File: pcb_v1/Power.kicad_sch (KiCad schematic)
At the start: 12 parts, among them J1 Conn_01x02, J2 Conn_01x04, U1 MAX17048G_T10, U5 TPB4056A20-ES1R

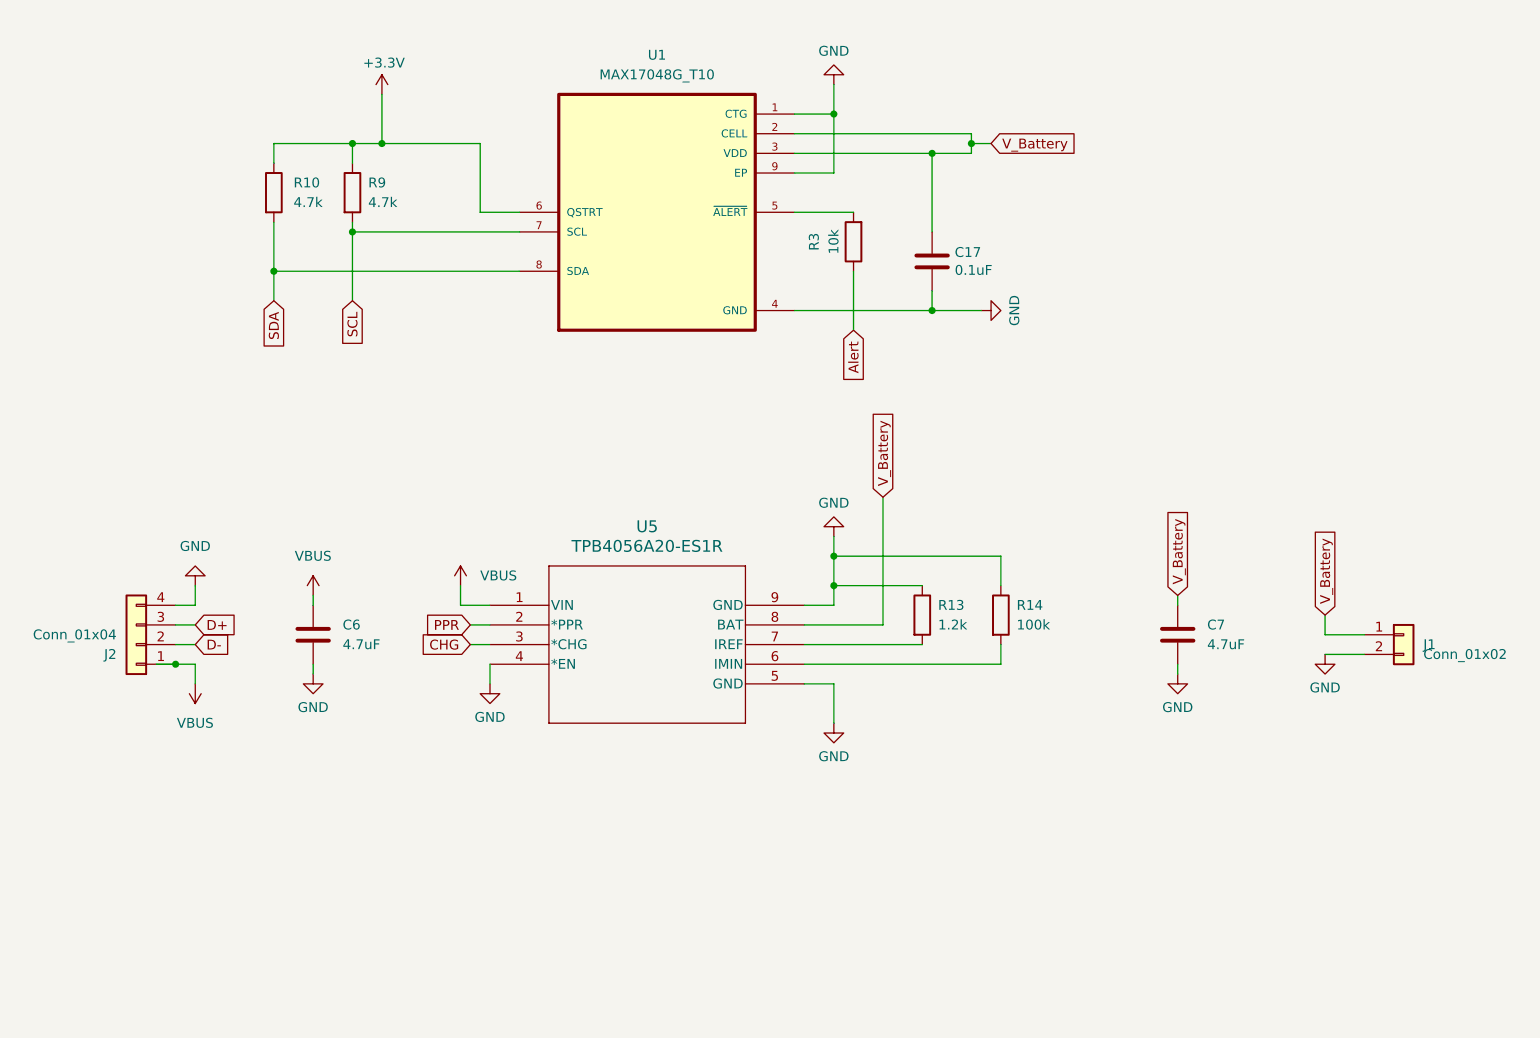
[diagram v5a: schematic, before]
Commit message: Finished 4 layer design
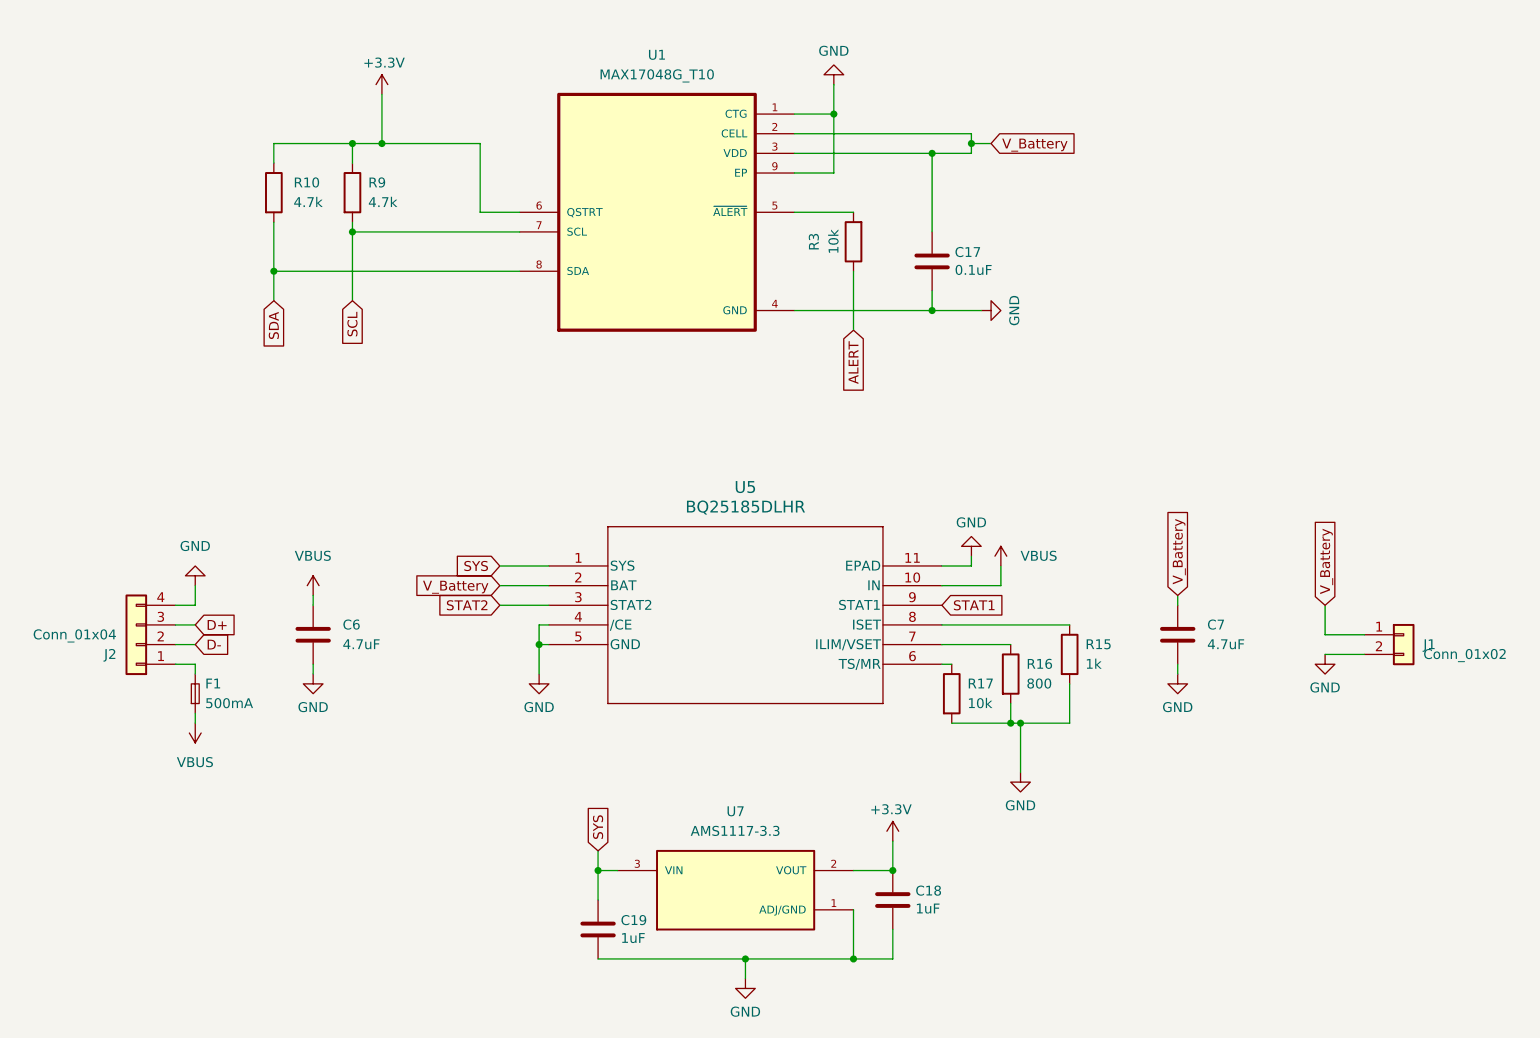
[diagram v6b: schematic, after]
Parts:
- removed R13: 1.2k, RC0402FR-7D4K7L:RESC1005X40N, symbol Device:R
- removed R14: 100k, RC0402FR-7D4K7L:RESC1005X40N, symbol Device:R
- removed U5: TPB4056A20-ES1R, TPB4056A20_ES1R:ESOP-8_TPK, symbol 2025-05-27_22-00-58:TPB4056A20-ES1R
- added C18, C19: 1uF, GRM1555C2A101GA01D:CAPC1005X55N, symbol Device:C
- added F1: 500mA, Fuse:Fuse_0603_1608Metric, symbol Device:Fuse_Small
- added R15: 1k, RC0402FR-7D4K7L:RESC1005X40N, symbol Device:R
- added R16: 800, RC0402FR-7D4K7L:RESC1005X40N, symbol Device:R
- added R17: 10k, RC0402FR-7D4K7L:RESC1005X40N, symbol Device:R
- added U5: BQ25185DLHR, footprints:WSON10_DLH_TEX, symbol BQ25185DLHR:BQ25185DLHR
- added U7: AMS1117-3.3, AMS1117-3.3:SOT229P700X180-4N, symbol AMS1117-3.3:AMS1117-3.3
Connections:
- net +3.3V: now also C18.1, U7.2 (VOUT)
- net GND: now also C18.2, C19.2, R15.2, R16.2, R17.2, U5.11 (EPAD), U5.4 (/CE), U5.5 (GND), U7.1 (ADJ/GND)
- net VBUS: now also F1.1, U5.10 (IN); no longer J2.1 (Pin_1)
- net V_Battery: now also U5.2 (BAT)
- net Alert renamed ALERT
- new net: R15.1, U5.8 (ISET)
- new net: R17.1, U5.6 (TS/MR)
- new net: F1.2, J2.1 (Pin_1)
- new net: R16.1, U5.7 (ILIM/VSET)
- new net STAT1: U5.9 (STAT1)
- new net STAT2: U5.3 (STAT2)
- new net SYS: C19.1, U5.1 (SYS), U7.3 (VIN)

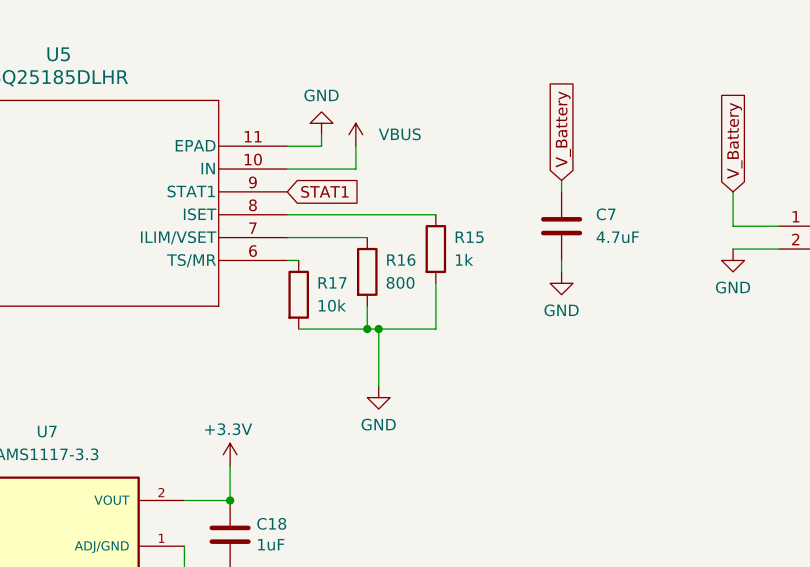
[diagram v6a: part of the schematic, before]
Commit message: Changed gasket mounts and added keepout zone for esp32
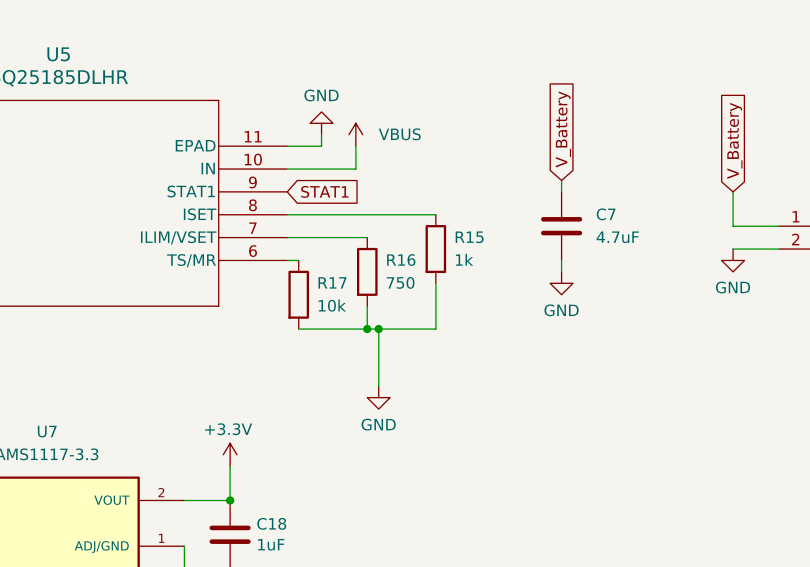
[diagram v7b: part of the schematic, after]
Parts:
- R16: value 800 -> 750
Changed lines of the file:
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@@
 			)
 		)
-		(property "Value" "800"
+		(property "Value" "750"
 			(at 169.672 116.84 0)
 			(effects

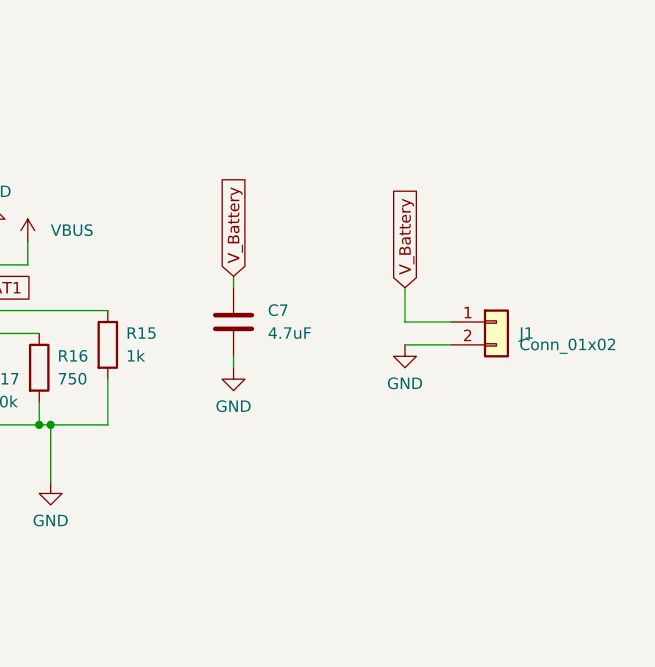
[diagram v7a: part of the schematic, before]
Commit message: Reverse polarity on pins
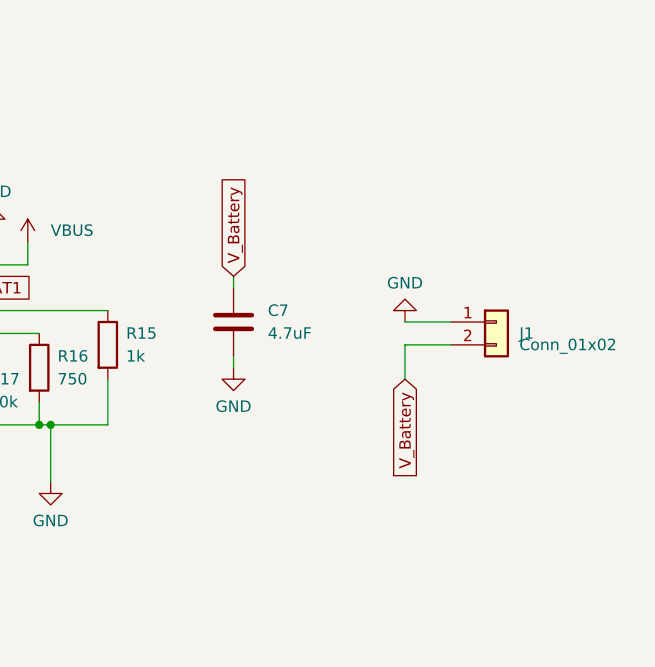
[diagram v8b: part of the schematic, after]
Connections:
- net GND: now also J1.1 (Pin_1); no longer J1.2 (Pin_2)
- net V_Battery: now also J1.2 (Pin_2); no longer J1.1 (Pin_1)
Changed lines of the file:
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@@
 	(wire
 		(pts
-			(xy 208.28 106.68) (xy 208.28 110.49)
+			(xy 86.36 40.64) (xy 86.36 46.99)
 		)
 		(stroke
@@
 	(wire
 		(pts
-			(xy 208.28 113.03) (xy 213.36 113.03)
+			(xy 152.4 152.4) (xy 147.32 152.4)
 		)
 		(stroke
@@
 	(wire
 		(pts
-			(xy 86.36 40.64) (xy 86.36 46.99)
+			(xy 175.26 121.92) (xy 175.26 116.84)
 		)
 		(stroke
@@
 	(wire
 		(pts
-			(xy 152.4 152.4) (xy 147.32 152.4)
+			(xy 72.39 67.31) (xy 72.39 63.5)
 		)
 		(stroke
@@
 	(wire
 		(pts
-			(xy 175.26 121.92) (xy 175.26 116.84)
+			(xy 168.91 121.92) (xy 175.26 121.92)
 		)
 		(stroke
@@
 	(wire
 		(pts
-			(xy 72.39 67.31) (xy 72.39 63.5)
+			(xy 208.28 110.49) (xy 213.36 110.49)
 		)
 		(stroke
@@
 	(wire
 		(pts
-			(xy 168.91 121.92) (xy 175.26 121.92)
+			(xy 158.75 111.76) (xy 167.64 111.76)
 		)
 		(stroke
@@
 	(wire
 		(pts
-			(xy 208.28 110.49) (xy 213.36 110.49)
+			(xy 208.28 113.03) (xy 213.36 113.03)
 		)
 		(stroke
@@
 	(wire
 		(pts
-			(xy 158.75 111.76) (xy 167.64 111.76)
+			(xy 166.37 104.14) (xy 158.75 104.14)
 		)
 		(stroke
@@
 	(wire
 		(pts
-			(xy 166.37 104.14) (xy 158.75 104.14)
+			(xy 101.6 106.68) (xy 107.95 106.68)
 		)
 		(stroke
@@
 	(wire
 		(pts
-			(xy 101.6 106.68) (xy 107.95 106.68)
+			(xy 101.6 104.14) (xy 107.95 104.14)
 		)
 		(stroke
@@
 	(wire
 		(pts
-			(xy 101.6 104.14) (xy 107.95 104.14)
+			(xy 133.35 154.94) (xy 133.35 152.4)
 		)
 		(stroke
@@
 	(wire
 		(pts
-			(xy 133.35 154.94) (xy 133.35 152.4)
+			(xy 99.06 55.88) (xy 104.14 55.88)
 		)
 		(stroke
@@
 	(wire
 		(pts
-			(xy 99.06 55.88) (xy 104.14 55.88)
+			(xy 77.47 115.57) (xy 77.47 114.3)
 		)
 		(stroke
@@
 	(wire
 		(pts
-			(xy 77.47 115.57) (xy 77.47 114.3)
+			(xy 157.48 68.58) (xy 139.7 68.58)
 		)
 		(stroke
@@
 	(wire
 		(pts
-			(xy 157.48 68.58) (xy 139.7 68.58)
+			(xy 208.28 116.84) (xy 208.28 113.03)
 		)
 		(stroke
@@
 		)
 	)
+	(global_label "V_Battery"
+		(shape input)
+		(at 208.28 116.84 270)
+		(fields_autoplaced yes)
+		(effects
+			(font
+				(size 1.27 1.27)
+			)
+			(justify right)
+		)
+		(property "Intersheetrefs" "${INTERSHEET_REFS}"
+			(at 208.28 128.5942 90)
+			(effects
+				(font
+					(size 1.27 1.27)
+				)
+				(justify right)
+				(hide yes)
+			)
+		)
+	)
 	(global_label "SCL"
 		(shape input)
@@
 		)
 	)
-	(global_label "V_Battery"
-		(shape input)
-		(at 208.28 106.68 90)
-		(fields_autoplaced yes)
-		(effects
-			(font
-				(size 1.27 1.27)
-			)
-			(justify left)
-		)
-		(property "Intersheetrefs" "${INTERSHEET_REFS}"
-			(at 208.28 94.9258 90)
-			(effects
-				(font
-					(size 1.27 1.27)
-				)
-				(justify left)
-				(hide yes)
-			)
-		)
-	)
 	(global_label "D-"
 		(shape input)
@@
 	(symbol
 		(lib_id "power:GND")
-		(at 208.28 113.03 0)
-		(mirror y)
+		(at 208.28 110.49 0)
+		(mirror x)
 		(unit 1)
 		(exclude_from_sim no)
@@
 		(dnp no)
 		(property "Reference" "#PWR0223"
-			(at 208.28 119.38 0)
+			(at 208.28 104.14 0)
 			(effects
 				(font
@@
 		)
 		(property "Value" "GND"
-			(at 208.28 117.348 0)
+			(at 208.28 106.172 0)
 			(effects
 				(font
@@
 		)
 		(property "Footprint" ""
-			(at 208.28 113.03 0)
+			(at 208.28 110.49 0)
 			(effects
 				(font
@@
 		)
 		(property "Datasheet" ""
-			(at 208.28 113.03 0)
+			(at 208.28 110.49 0)
 			(effects
 				(font
@@
 		)
 		(property "Description" ""
-			(at 208.28 113.03 0)
-			(effects
-				(font
+			(at 208.28 110.49 0)
+			(effects
+				(font
